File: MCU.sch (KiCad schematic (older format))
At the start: 11 parts

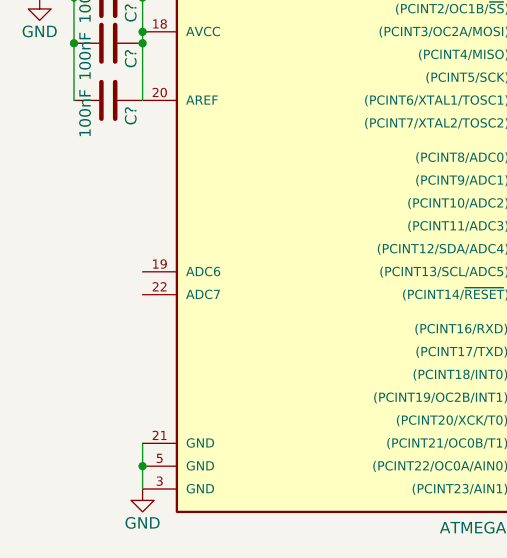
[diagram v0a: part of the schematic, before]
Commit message: Did power and encoder
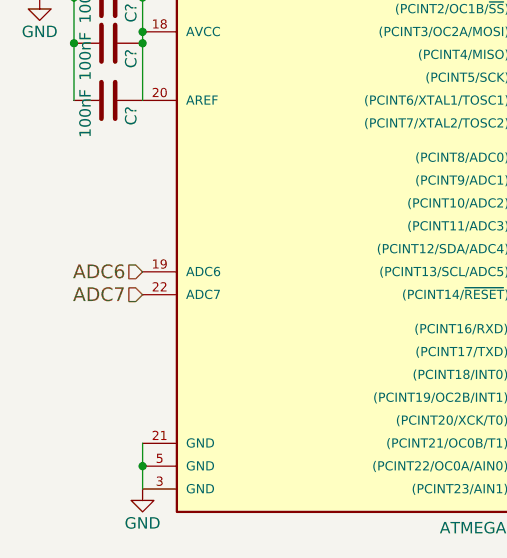
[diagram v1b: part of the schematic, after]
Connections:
- net ADC6: now reaches U?.19 (ADC6)
- net ADC7: now reaches U?.22 (ADC7)
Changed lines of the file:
@@
 LIBS:contrib
 LIBS:valves
-LIBS:testpart
+LIBS:CustomComponents
 LIBS:roller_blade-cache
 EELAYER 25 0
@@
 Text HLabel 3850 1500 2    60   Input ~ 0
 PB2
+Text HLabel 1950 2650 0    60   Input ~ 0
+ADC6
+Text HLabel 1950 2750 0    60   Input ~ 0
+ADC7
 $EndSCHEMATC
